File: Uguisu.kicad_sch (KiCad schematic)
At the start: 8 parts, among them U1 XIAO-nRF52840-SMD

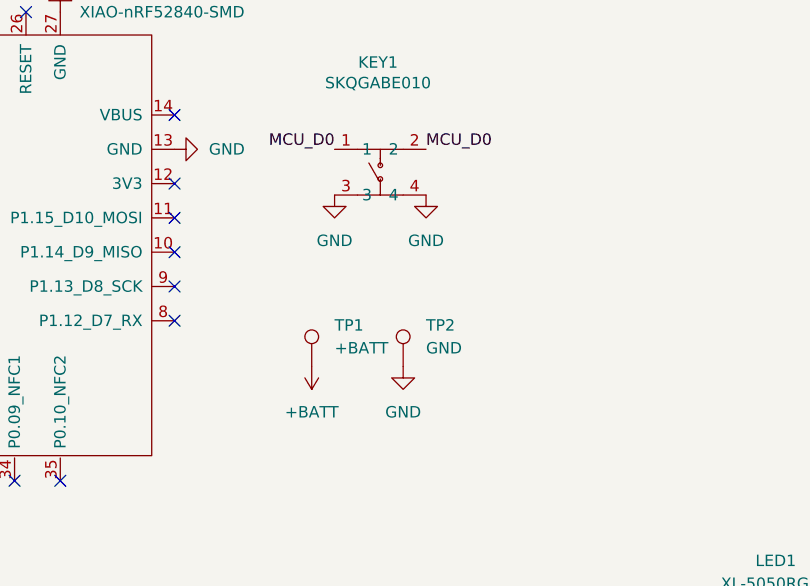
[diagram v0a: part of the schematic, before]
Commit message: hw: add 3.3V and GND test point pads for AirTag power tap
- Label U1 3V3 pin as /3.3V net (was unconnected)
- Add 3x3mm SMD test point pads for 3.3V and GND adjacent to XIAO
- Rename existing BATT/GND test points with clearer silkscreen labels
- Route 3.3V net to test point via back copper
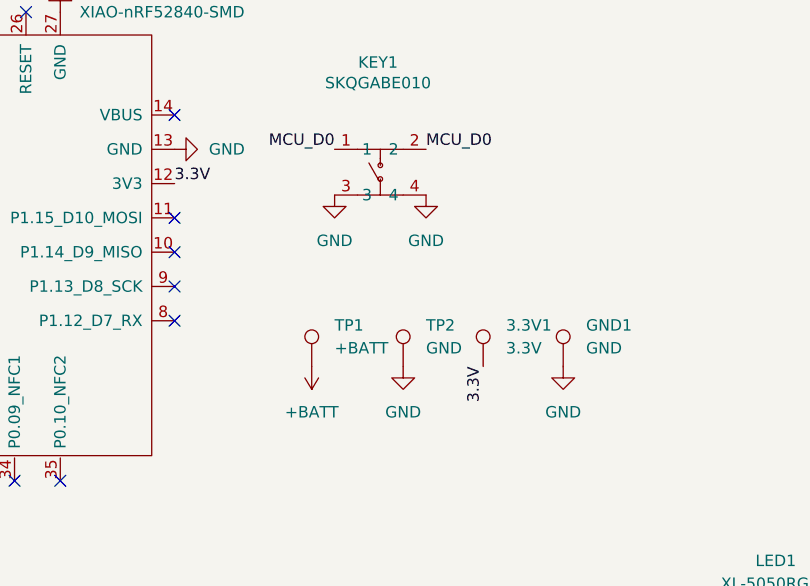
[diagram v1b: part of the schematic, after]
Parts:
- added 3.3V1: 3.3V, TestPoint:TestPoint_Pad_3.0x3.0mm, symbol Connector:TestPoint
- added GND1: GND, TestPoint:TestPoint_Pad_3.0x3.0mm, symbol Connector:TestPoint
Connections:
- net GND: now also GND1.1
- net 3.3V: now reaches U1.12 (3V3)
- net 3.3V: now also 3.3V1.1
- no-connect marks 14 -> 13
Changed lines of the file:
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@@
-	)
-	(no_connect
-		(at 85.09 63.5)
 	)
 	(no_connect
@@
 		)
 	)
+	(label "3.3V"
+		(at 85.09 63.5 0)
+		(effects
+			(font
+				(size 1.27 1.27)
+			)
+			(justify left bottom)
+		)
+	)
 	(label "MCU_D3"
 		(at 163.83 111.76 0)
@@
 		)
 	)
+	(label "3.3V"
+		(at 119.38 83.82 270)
+		(effects
+			(font
+				(size 1.27 1.27)
+			)
+			(justify right bottom)
+		)
+	)
 	(label "MCU_D1"
 		(at 163.83 121.92 0)
@@
 	)
 	(symbol
+		(lib_id "power:GND")
+		(at 128.27 83.82 0)
+		(unit 1)
+		(exclude_from_sim no)
+		(in_bom yes)
+		(on_board yes)
+		(dnp no)
+		(fields_autoplaced yes)
+		(property "Reference" "#PWR09"
+			(at 128.27 90.17 0)
+			(effects
+				(font
+					(size 1.27 1.27)
+				)
+				(hide yes)
+			)
+		)
+		(property "Value" "GND"
+			(at 128.27 88.9 0)
+			(effects
+				(font
+					(size 1.27 1.27)
+				)
+			)
+		)
+		(property "Footprint" ""
+			(at 128.27 83.82 0)
+			(effects
+				(font
+					(size 1.27 1.27)
+				)
+				(hide yes)
+			)
+		)
+		(property "Datasheet" ""
+			(at 128.27 83.82 0)
+			(effects
+				(font
+					(size 1.27 1.27)
+				)
+				(hide yes)
+			)
+		)
+		(property "Description" "Power symbol creates a global label with name \"GND\" , ground"
+			(at 128.27 83.82 0)
+			(effects
+				(font
+					(size 1.27 1.27)
+				)
+				(hide yes)
+			)
+		)
+		(pin "1"
+		)
+		(instances
+			(project ""
+				(path "/3411fae6-0f44-4a47-8bb3-5970407324d6"
+					(reference "#PWR09")
+					(unit 1)
+				)
+			)
+		)
+	)
+	(symbol
 		(lib_id "power:+BATT")
 		(at 143.51 116.84 90)
@@
 	)
 	(symbol
+		(lib_id "Connector:TestPoint")
+		(at 128.27 83.82 0)
+		(unit 1)
+		(exclude_from_sim no)
+		(in_bom yes)
+		(on_board yes)
+		(dnp no)
+		(fields_autoplaced yes)
+		(property "Reference" "GND1"
+			(at 130.81 79.2479 0)
+			(effects
+				(font
+					(size 1.27 1.27)
+				)
+				(justify left)
+			)
+		)
+		(property "Value" "GND"
+			(at 130.81 81.7879 0)
+			(effects
+				(font
+					(size 1.27 1.27)
+				)
+				(justify left)
+			)
+		)
+		(property "Footprint" "TestPoint:TestPoint_Pad_3.0x3.0mm"
+			(at 133.35 83.82 0)
+			(effects
+				(font
+					(size 1.27 1.27)
+				)
+				(hide yes)
+			)
+		)
+		(property "Datasheet" "~"
+			(at 133.35 83.82 0)
+			(effects
+				(font
+					(size 1.27 1.27)
+				)
+				(hide yes)
+			)
+		)
+		(property "Description" "test point"
+			(at 128.27 83.82 0)
+			(effects
+				(font
+					(size 1.27 1.27)
+				)
+				(hide yes)
+			)
+		)
+		(pin "1"
+		)
+		(instances
+			(project ""
+				(path "/3411fae6-0f44-4a47-8bb3-5970407324d6"
+					(reference "GND1")
+					(unit 1)
+				)
+			)
+		)
+	)
+	(symbol
 		(lib_id "power:GND")
 		(at 85.09 59.69 90)
@@
 					(unit 1)
 				)
+			)
+		)
+	)
+	(symbol
+		(lib_id "Connector:TestPoint")
+		(at 119.38 83.82 0)
+		(unit 1)
+		(exclude_from_sim no)
+		(in_bom yes)
+		(on_board yes)
+		(dnp no)
+		(fields_autoplaced yes)
+		(property "Reference" "3.3V1"
+			(at 121.92 79.2479 0)
+			(effects
+				(font
+					(size 1.27 1.27)
+				)
+				(justify left)
+			)
+		)
+		(property "Value" "3.3V"
+			(at 121.92 81.7879 0)
+			(effects
+				(font
+					(size 1.27 1.27)
+				)
+				(justify left)
+			)
+		)
+		(property "Footprint" "TestPoint:TestPoint_Pad_3.0x3.0mm"
+			(at 124.46 83.82 0)
+			(effects
+				(font
+					(size 1.27 1.27)
+				)
+				(hide yes)
+			)
+		)
+		(property "Datasheet" "~"
+			(at 124.46 83.82 0)
+			(effects
+				(font
+					(size 1.27 1.27)
+				)
+				(hide yes)
+			)
+		)
+		(property "Description" "test point"
+			(at 119.38 83.82 0)
+			(effects
+				(font
+					(size 1.27 1.27)
+				)
+				(hide yes)
+			)
+		)
+		(pin "1"
+		)
+		(instances
+			(project ""
+				(path "/3411fae6-0f44-4a47-8bb3-5970407324d6"
+					(reference "3.3V1")
+					(unit 1)
+				)
